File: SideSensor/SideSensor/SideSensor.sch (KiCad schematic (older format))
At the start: 6 parts, among them J1 SH_03, U1 S7136

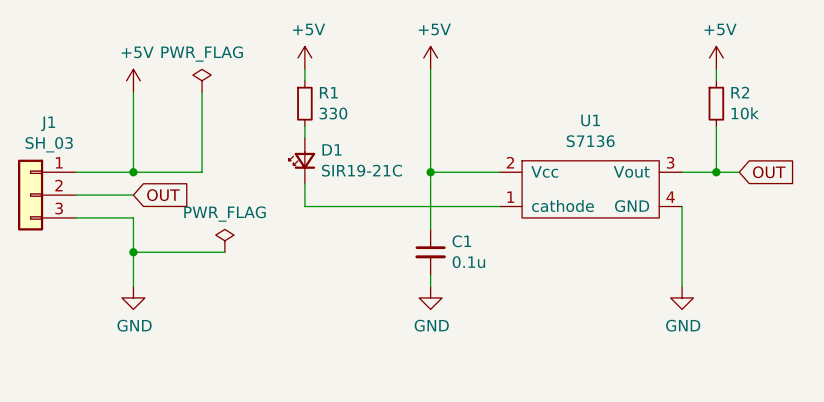
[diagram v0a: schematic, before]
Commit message: add logo
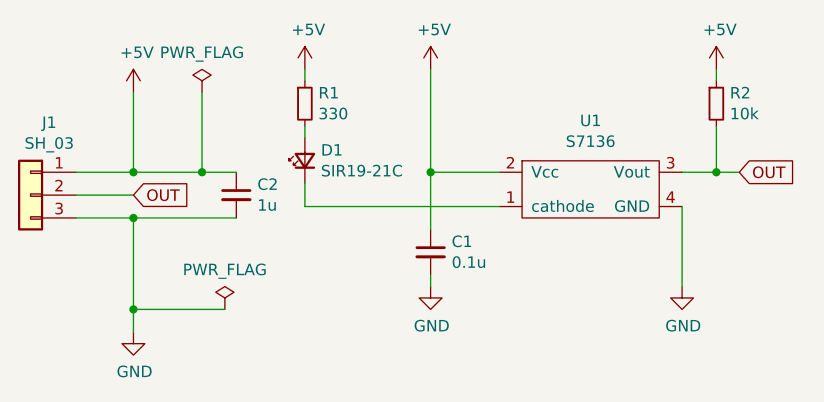
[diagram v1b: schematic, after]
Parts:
- added C2: 1u, symbol Device:C_Small
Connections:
- net +5V: now also C2.1
- net GND: now also C2.2
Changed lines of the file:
@@
 L power:GND #PWR05
 U 1 1 60AAF0F8
-P 4650 4350
-F 0 "#PWR05" H 4650 4100 50  0001 C CNN
-F 1 "GND" H 4655 4177 50  0000 C CNN
-F 2 "" H 4650 4350 50  0001 C CNN
-F 3 "" H 4650 4350 50  0001 C CNN
-	1    4650 4350
+P 4650 4550
+F 0 "#PWR05" H 4650 4300 50  0001 C CNN
+F 1 "GND" H 4655 4377 50  0000 C CNN
+F 2 "" H 4650 4550 50  0001 C CNN
+F 3 "" H 4650 4550 50  0001 C CNN
+	1    4650 4550
 	1    0    0    -1
 $EndComp
 Wire Wire Line
-	4650 4350 4650 4200
+	4650 4550 4650 4450
 Wire Wire Line
 	4650 4050 4400 4050
@@
 L power:PWR_FLAG #FLG02
 U 1 1 60AB8F73
-P 5050 4200
-F 0 "#FLG02" H 5050 4275 50  0001 C CNN
-F 1 "PWR_FLAG" H 5050 4373 50  0000 C CNN
-F 2 "" H 5050 4200 50  0001 C CNN
-F 3 "~" H 5050 4200 50  0001 C CNN
-	1    5050 4200
+P 5050 4450
+F 0 "#FLG02" H 5050 4525 50  0001 C CNN
+F 1 "PWR_FLAG" H 5050 4623 50  0000 C CNN
+F 2 "" H 5050 4450 50  0001 C CNN
+F 3 "~" H 5050 4450 50  0001 C CNN
+	1    5050 4450
 	1    0    0    -1
 $EndComp
-Connection ~ 4650 4200
+Connection ~ 4650 4450
 Wire Wire Line
-	4650 4200 4650 4050
+	4650 4450 4650 4050
 Wire Wire Line
-	4650 4200 5050 4200
+	4650 4450 5050 4450
+$Comp
+L Device:C_Small C2
+U 1 1 6110F7F0
+P 5100 3950
+F 0 "C2" H 5192 3996 50  0000 L CNN
+F 1 "1u" H 5192 3905 50  0000 L CNN
+F 2 "" H 5100 3950 50  0001 C CNN
+F 3 "~" H 5100 3950 50  0001 C CNN
+	1    5100 3950
+	1    0    0    -1
+$EndComp
+Wire Wire Line
+	4950 3850 5100 3850
+Connection ~ 4950 3850
+Wire Wire Line
+	5100 4050 4650 4050
+Connection ~ 4650 4050
 $EndSCHEMATC

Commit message: complete
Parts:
- C2: footprint (none) -> Capacitor_SMD:C_0603_1608Metric
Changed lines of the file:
@@
 F 0 "C2" H 5192 3996 50  0000 L CNN
 F 1 "1u" H 5192 3905 50  0000 L CNN
-F 2 "" H 5100 3950 50  0001 C CNN
+F 2 "Capacitor_SMD:C_0603_1608Metric" H 5100 3950 50  0001 C CNN
 F 3 "~" H 5100 3950 50  0001 C CNN
 	1    5100 3950

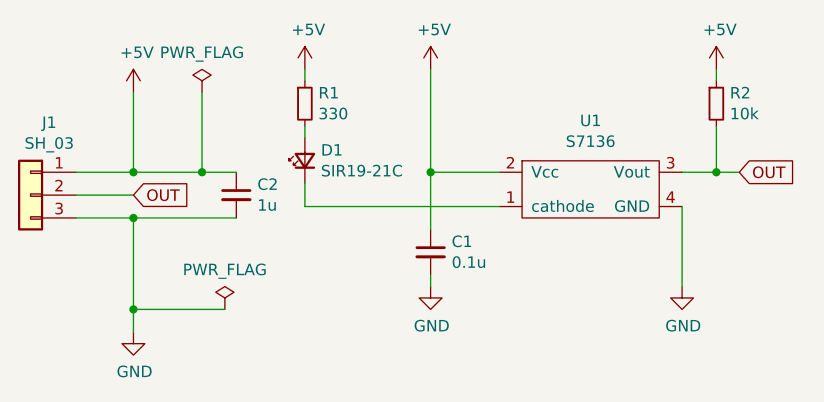
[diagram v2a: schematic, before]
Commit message: センサの抵抗値などを変更
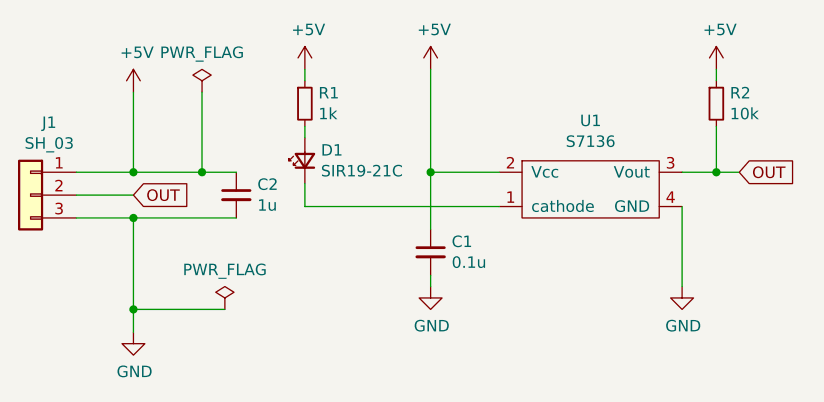
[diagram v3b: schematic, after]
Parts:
- R1: value 330 -> 1k
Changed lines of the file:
@@
 P 5400 3550
 F 0 "R1" H 5459 3596 50  0000 L CNN
-F 1 "330" H 5459 3505 50  0000 L CNN
+F 1 "1k" H 5459 3505 50  0000 L CNN
 F 2 "Resistor_SMD:R_0603_1608Metric" H 5400 3550 50  0001 C CNN
 F 3 "~" H 5400 3550 50  0001 C CNN
